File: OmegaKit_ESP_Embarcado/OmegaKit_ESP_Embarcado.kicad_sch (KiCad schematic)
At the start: 24 parts, among them J1 USB_B_Micro, J10 QTR_2, J11 SERVO1, J12 SERVO2, J2 MOTOR_B, J3 SENSOR_2, J4 SENSOR_1, J5 MOTOR_A, J6 SENSOR_3, J7 SENSOR_4, J8 SENSOR_5, J9 QTR_1, SW1 SW_Push, SW2 SW_Push, U1 CP2102N-Axx-xQFN28, U2 TB6612FNG, U3 ESP32-WROOM-32, U4 TSOP1838, U5 AMS1117-3.3

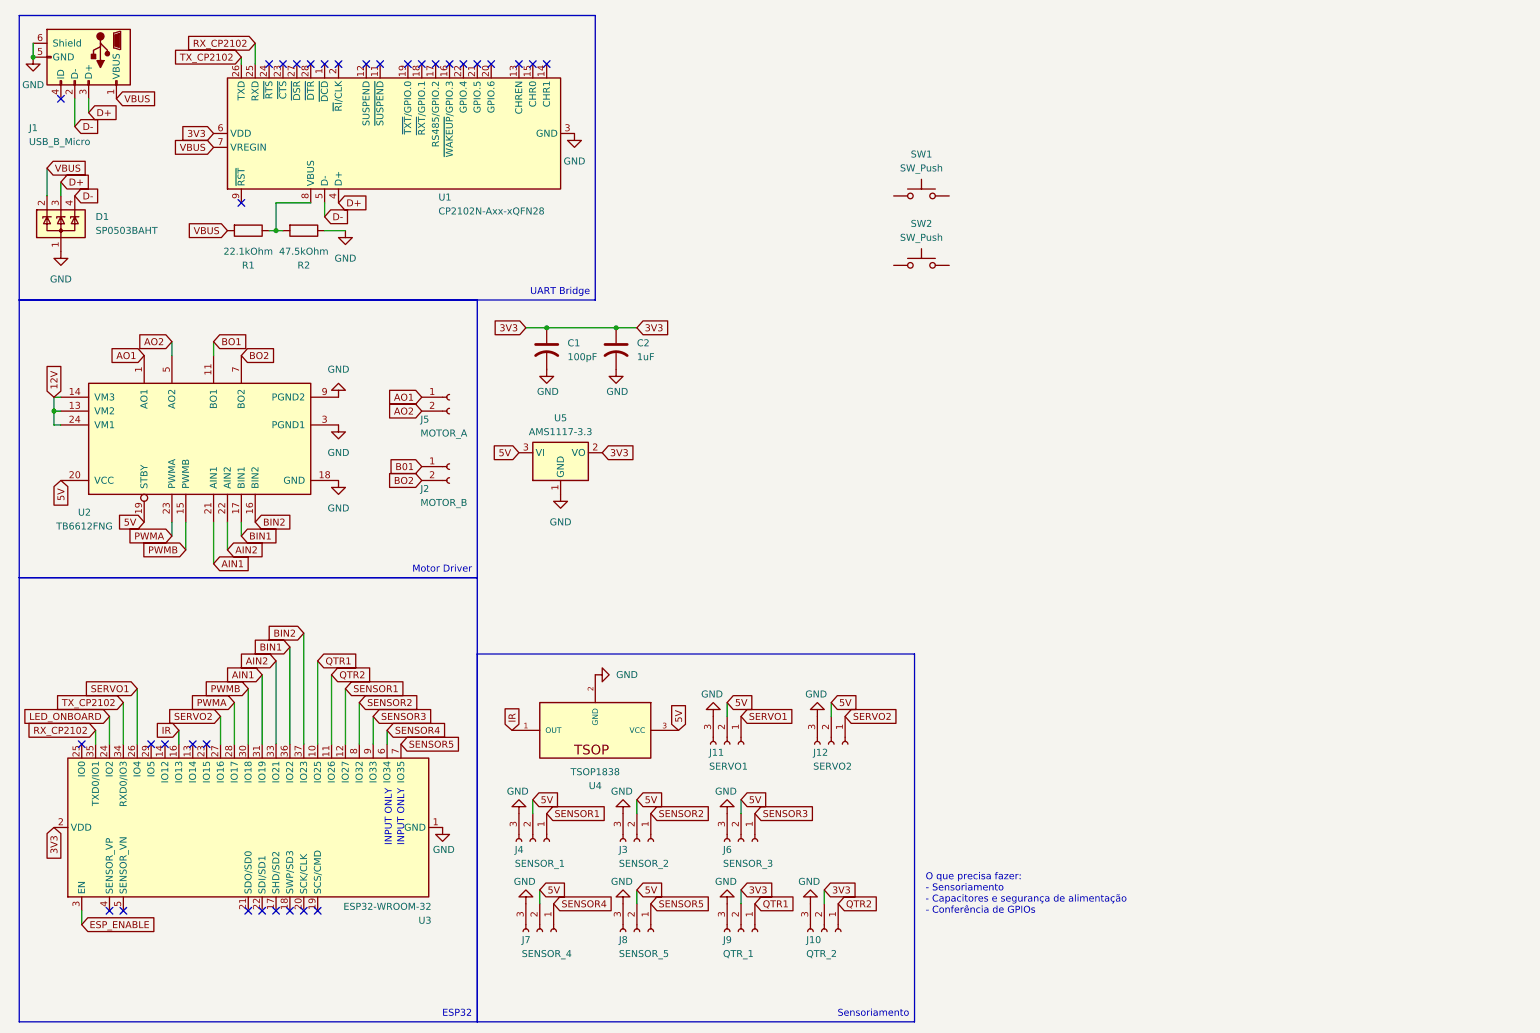
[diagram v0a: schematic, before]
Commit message: ✨🚧 feat(Omegakit_ESP_Embarcado/*): Inicia desenho da PCB
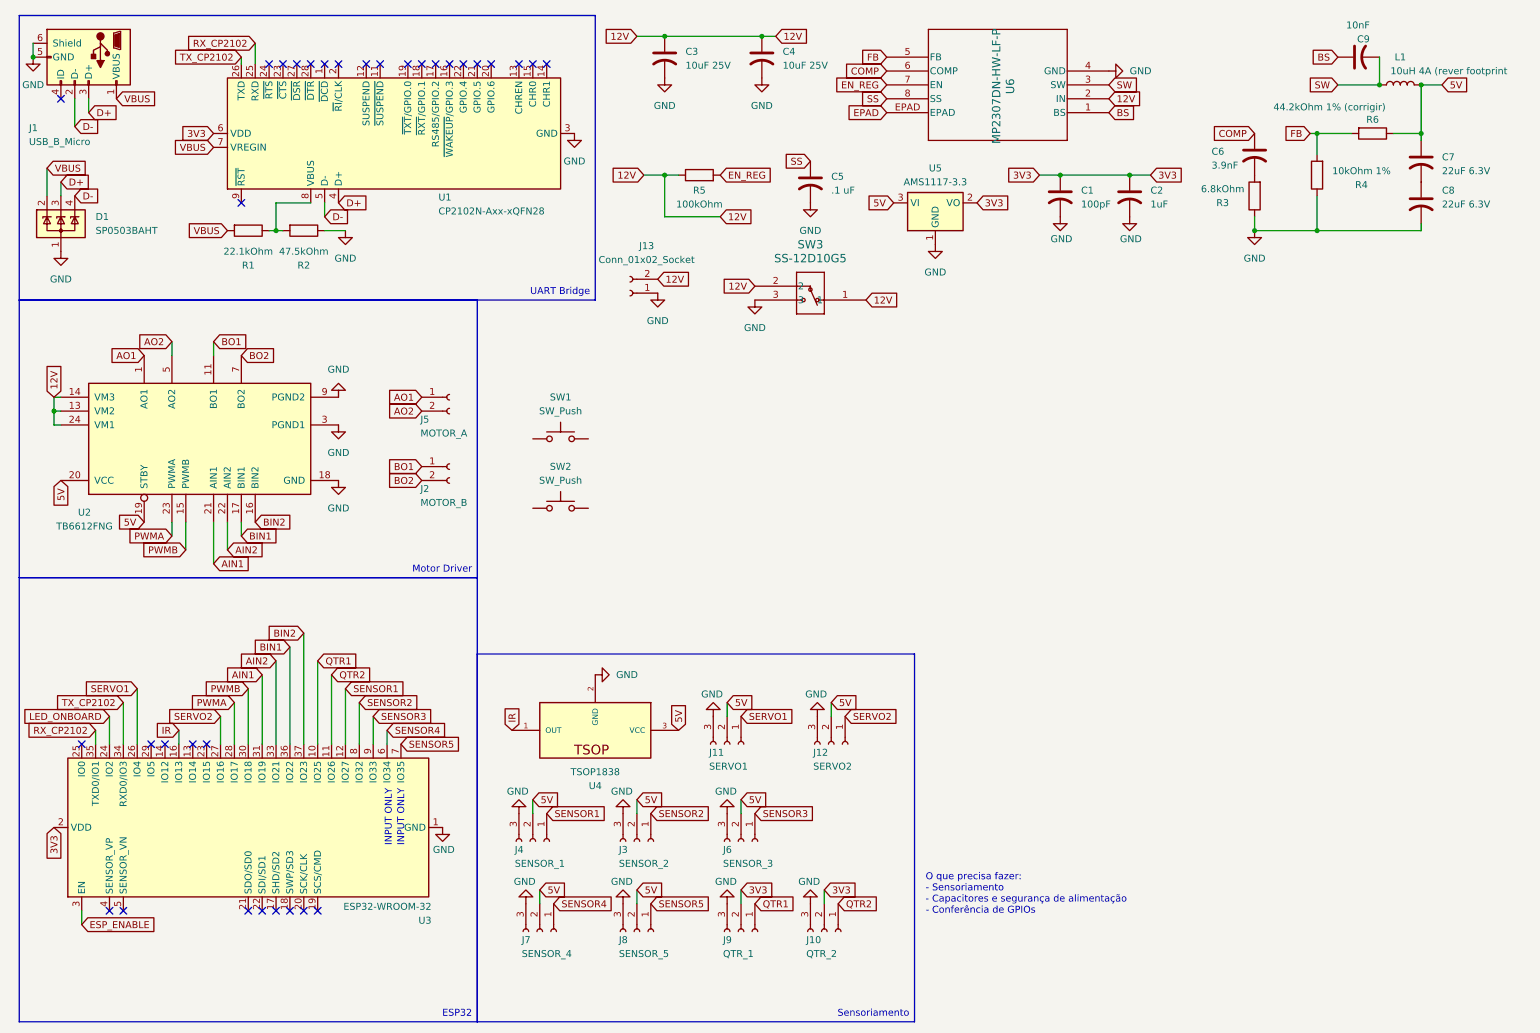
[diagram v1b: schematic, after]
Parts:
- added C3, C4: 10uF 25V, Capacitor_SMD:C_Elec_3x5.4, symbol Device:C_US
- added C5: .1 uF, Capacitor_SMD:C_0201_0603Metric_Pad0.64x0.40mm_HandSolder, symbol Device:C_US
- added C6: 3.9nF, Capacitor_SMD:C_0402_1005Metric_Pad0.74x0.62mm_HandSolder, symbol Device:C_US
- added C7, C8: 22uF 6.3V, Capacitor_SMD:C_1206_3216Metric_Pad1.33x1.80mm_HandSolder, symbol Device:C_US
- added C9: 10nF, Capacitor_SMD:C_0805_2012Metric_Pad1.18x1.45mm_HandSolder, symbol Device:C_US
- added J13: Conn_01x02_Socket, Connector_PinHeader_2.54mm:PinHeader_1x02_P2.54mm_Vertical, symbol Connector:Conn_01x02_Socket
- added L1: 10uH 4A (rever footprint, Inductor_SMD:L_Neosid_SM-PIC0512H, symbol Device:L
- added R3: 6.8kOhm, Resistor_SMD:R_0201_0603Metric_Pad0.64x0.40mm_HandSolder, symbol Device:R
- added R4: 10kOhm 1%, Resistor_SMD:R_0201_0603Metric_Pad0.64x0.40mm_HandSolder, symbol Device:R
- added R5: 100kOhm, Resistor_SMD:R_0201_0603Metric_Pad0.64x0.40mm_HandSolder, symbol Device:R
- added R6: 44.2kOhm 1% (corrigir), Resistor_SMD:R_0201_0603Metric_Pad0.64x0.40mm_HandSolder, symbol Device:R
- added SW3: SS-12D10G5, footprints:SS-12D10G5_XKB, symbol SS-12D10G5:SS-12D10G5
- added U6: MP2307DN-HW-LF-P, IC8_MP2307_MNP, symbol MP2307DN-HW-LF-P:MP2307DN-HW-LF-P
- C1: footprint (none) -> Capacitor_SMD:C_0603_1608Metric_Pad1.08x0.95mm_HandSolder
- C2: footprint (none) -> Capacitor_SMD:C_0402_1005Metric_Pad0.74x0.62mm_HandSolder
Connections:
- net B01 is gone; now on net BO1: J2.1 (Pin_1)
- net 12V: now also C3.1, C4.1, J13.2 (Pin_2), R5.1, SW3.1, SW3.2, U6.2 (IN)
- net 5V: now also C7.1, L1.2, R6.1
- net GND: now also C3.2, C4.2, C5.2, C8.2, J13.1 (Pin_1), R3.1, R4.1, SW3.3, U6.4 (GND)
- new net: C6.2, R3.2
- new net: C7.2, C8.1
- new net BS: C9.1, U6.1 (BS)
- new net COMP: C6.1, U6.6 (COMP)
- new net EN_REG: R5.2, U6.7 (EN)
- new net EPAD: U6.EPAD
- new net FB: R4.2, R6.2, U6.5 (FB)
- new net SS: C5.1, U6.8 (SS)
- new net SW: C9.2, L1.1, U6.3 (SW)
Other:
- moved on the sheet: C1, C2, SW1, SW2, U5

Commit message: ✨🚧 feat(OmegaKit_ESP_Embarcado/*): Monta primeira versão da placa, revisa circuitos, remove CP2102
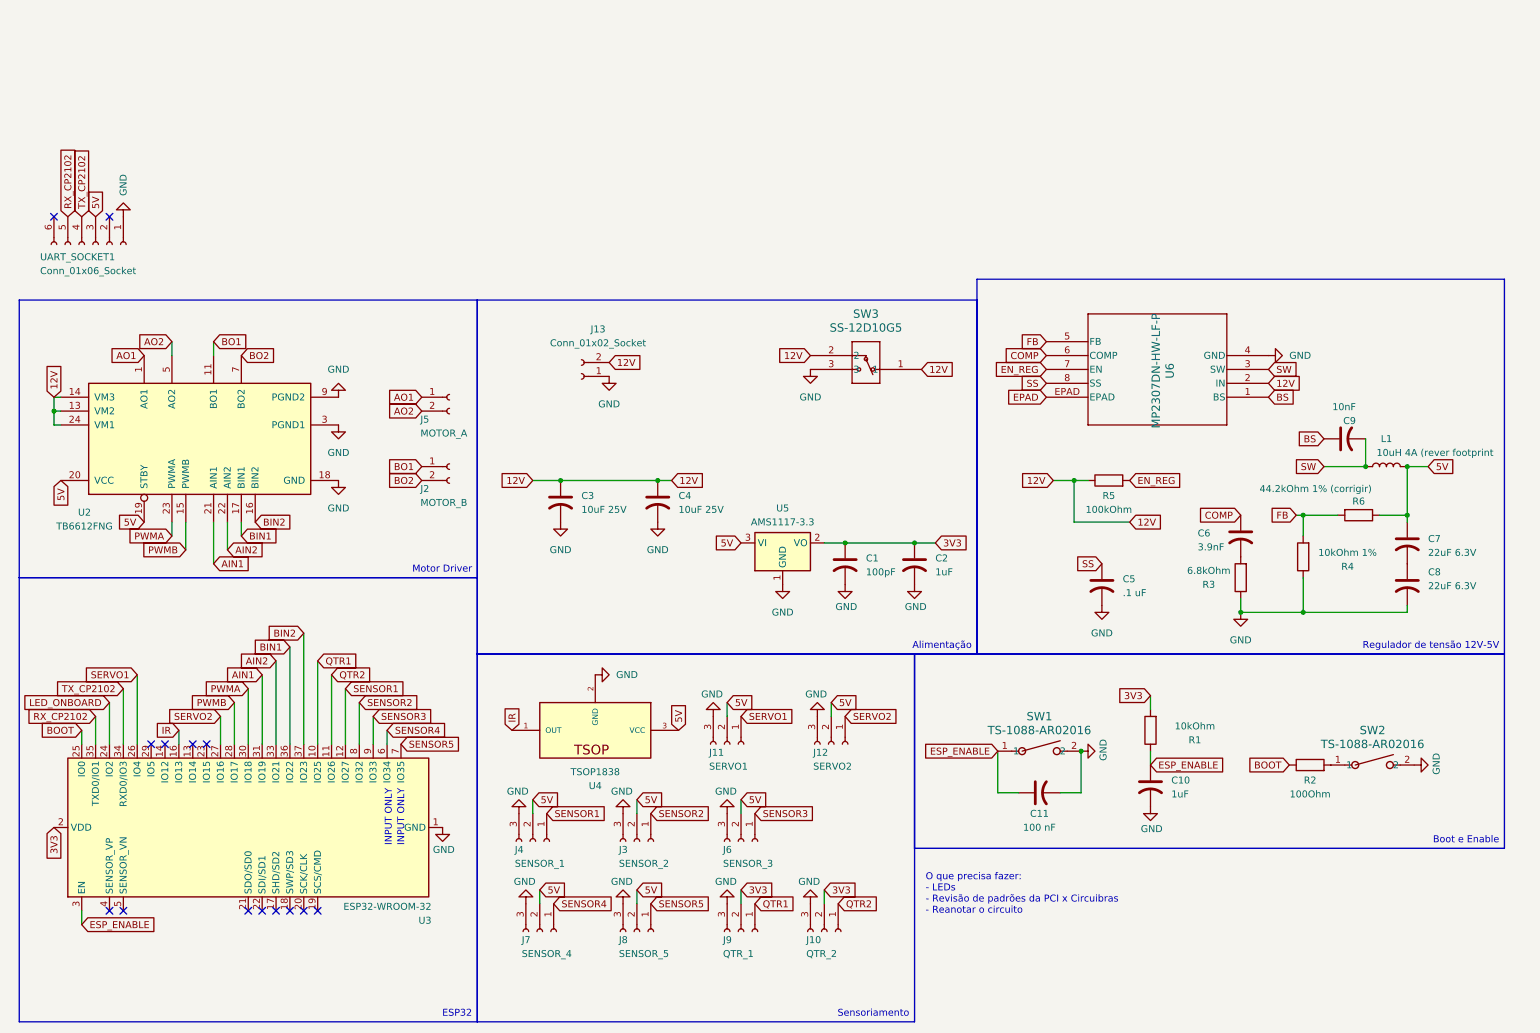
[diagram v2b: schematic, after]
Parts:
- removed D1: SP0503BAHT, Package_TO_SOT_SMD:SOT-143, symbol Power_Protection:SP0503BAHT
- removed J1: USB_B_Micro, Connector_USB:USB_Micro-AB_Molex_47590-0001, symbol Connector:USB_B_Micro
- removed SW1, SW2: SW_Push, symbol Switch:SW_Push
- removed U1: CP2102N-Axx-xQFN28, Package_DFN_QFN:QFN-28-1EP_5x5mm_P0.5mm_EP3.35x3.35mm, symbol Interface_USB:CP2102N-Axx-xQFN28
- added C10: 1uF, Capacitor_SMD:C_0402_1005Metric_Pad0.74x0.62mm_HandSolder, symbol Device:C_US
- added C11: 100 nF, Capacitor_SMD:C_0201_0603Metric_Pad0.64x0.40mm_HandSolder, symbol Device:C_US
- added SW1, SW2: TS-1088-AR02016, SW_TS-1088_XNP, symbol TS-1088-ARO2016:TS-1088-AR02016
- added UART_SOCKET1: Conn_01x06_Socket, Connector_PinHeader_2.54mm:PinHeader_1x06_P2.54mm_Vertical, symbol Connector:Conn_01x06_Socket
- C7, C8: footprint Capacitor_SMD:C_1206_3216Metric_Pad1.33x1.80mm_HandSolder -> Capacitor_SMD:C_0603_1608Metric_Pad1.08x0.95mm_HandSolder
- C9: footprint Capacitor_SMD:C_0805_2012Metric_Pad1.18x1.45mm_HandSolder -> Capacitor_SMD:C_0504_1310Metric_Pad0.83x1.28mm_HandSolder
- R1: value 22.1kOhm -> 10kOhm; footprint Resistor_SMD:R_0201_0603Metric_Pad0.64x0.40mm_HandSolder -> Resistor_SMD:R_0603_1608Metric_Pad0.98x0.95mm_HandSolder
- R2: value 47.5kOhm -> 100Ohm; footprint Resistor_SMD:R_0201_0603Metric_Pad0.64x0.40mm_HandSolder -> Resistor_SMD:R_0805_2012Metric_Pad1.20x1.40mm_HandSolder
- R4, R6: footprint Resistor_SMD:R_0201_0603Metric_Pad0.64x0.40mm_HandSolder -> Resistor_SMD:R_0603_1608Metric_Pad0.98x0.95mm_HandSolder
- R5: footprint Resistor_SMD:R_0201_0603Metric_Pad0.64x0.40mm_HandSolder -> Resistor_SMD:R_0805_2012Metric_Pad1.20x1.40mm_HandSolder
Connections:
- net VBUS is gone; now on net 3V3: R1.2
- net 5V: now also UART_SOCKET1.3 (Pin_3)
- net ESP_ENABLE: now also R1.1, C10.1, C11.1, SW1.1
- net GND: now also C10.2, C11.2, SW1.2, SW2.2, UART_SOCKET1.1 (Pin_1); no longer R2.1
- net PWMA: now also U3.30 (IO18); no longer U3.28 (IO17)
- net PWMB: now also U3.28 (IO17); no longer U3.30 (IO18)
- net RX_CP2102: now also UART_SOCKET1.5 (Pin_5)
- net TX_CP2102: now also UART_SOCKET1.4 (Pin_4)
- net at R2.2: now also SW2.1; no longer R1.1
- net BOOT: now reaches U3.25 (IO0)
- net BOOT: now also R2.1
- no-connect marks 33 -> 14
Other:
- note added: "O que precisa fazer: - LEDs - Revisão de padrões da PCI x Circuibras - Reanotar o circuito"
- note removed: "O que precisa fazer: - Sensoriamento - Capacitores e segurança de alimentação - Conferência de GPIOs"
- moved on the sheet: C1, C2, C3, C4, C5, C6, C7, C8, C9, J13, L1, R3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

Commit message: ✨ feat(OmegaKit_ESP_Embarcado/*): Adiciona LEDs nos sensores e LED de energia, muda footprint dos capacitores da bateria
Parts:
- added D1, D2, D3, D4, D5, D6, D7: LED, LED_SMD:LED_0805_2012Metric_Pad1.15x1.40mm_HandSolder, symbol Device:LED
- added R10, R11, R12, R7, R8, R9: 220Ohm, Resistor_SMD:R_0805_2012Metric_Pad1.20x1.40mm_HandSolder, symbol Device:R
- added R13: 1KOhm, Resistor_SMD:R_0805_2012Metric_Pad1.20x1.40mm_HandSolder, symbol Device:R
- C1: renamed from C3; footprint Capacitor_SMD:C_Elec_3x5.4 -> Capacitor_SMD:C_Elec_4x5.4
- C2: renamed from C4; footprint Capacitor_SMD:C_Elec_3x5.4 -> Capacitor_SMD:C_Elec_4x5.4
- renumbered C1 to C3, C2 to C4, U4 to IR13, J9 to Q25, J10 to Q26, J4 to S27, J3 to S32, J6 to S33, J7 to S34, J8 to S35, J12 to SERVO16, J11 to SERVO4
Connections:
- net 3V3: now also R13.1
- net GND: now also D1.1 (K), D7.1 (K)
- net LED_ONBOARD: now also R7.1
- net SENSOR1: now also D2.1 (K), R8.1
- net SENSOR2: now also D4.1 (K), R10.1
- net SENSOR3: now also D6.1 (K), R12.1
- net SENSOR4: now also D5.1 (K), R11.1
- net SENSOR5: now also D3.1 (K), R9.1
- new net: D4.2 (A), R10.2
- new net: D5.2 (A), R11.2
- new net: D6.2 (A), R12.2
- new net: D3.2 (A), R9.2
- new net: D2.2 (A), R8.2
- new net: D7.2 (A), R13.2
- new net: D1.2 (A), R7.2
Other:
- note added: "O que precisa fazer: - Rever padrões Circuibras - Rever valores (fazer contaKKKKKKKKKKKKKKK)"
- note removed: "O que precisa fazer: - LEDs - Revisão de padrões da PCI x Circuibras - Reanotar o circuito"

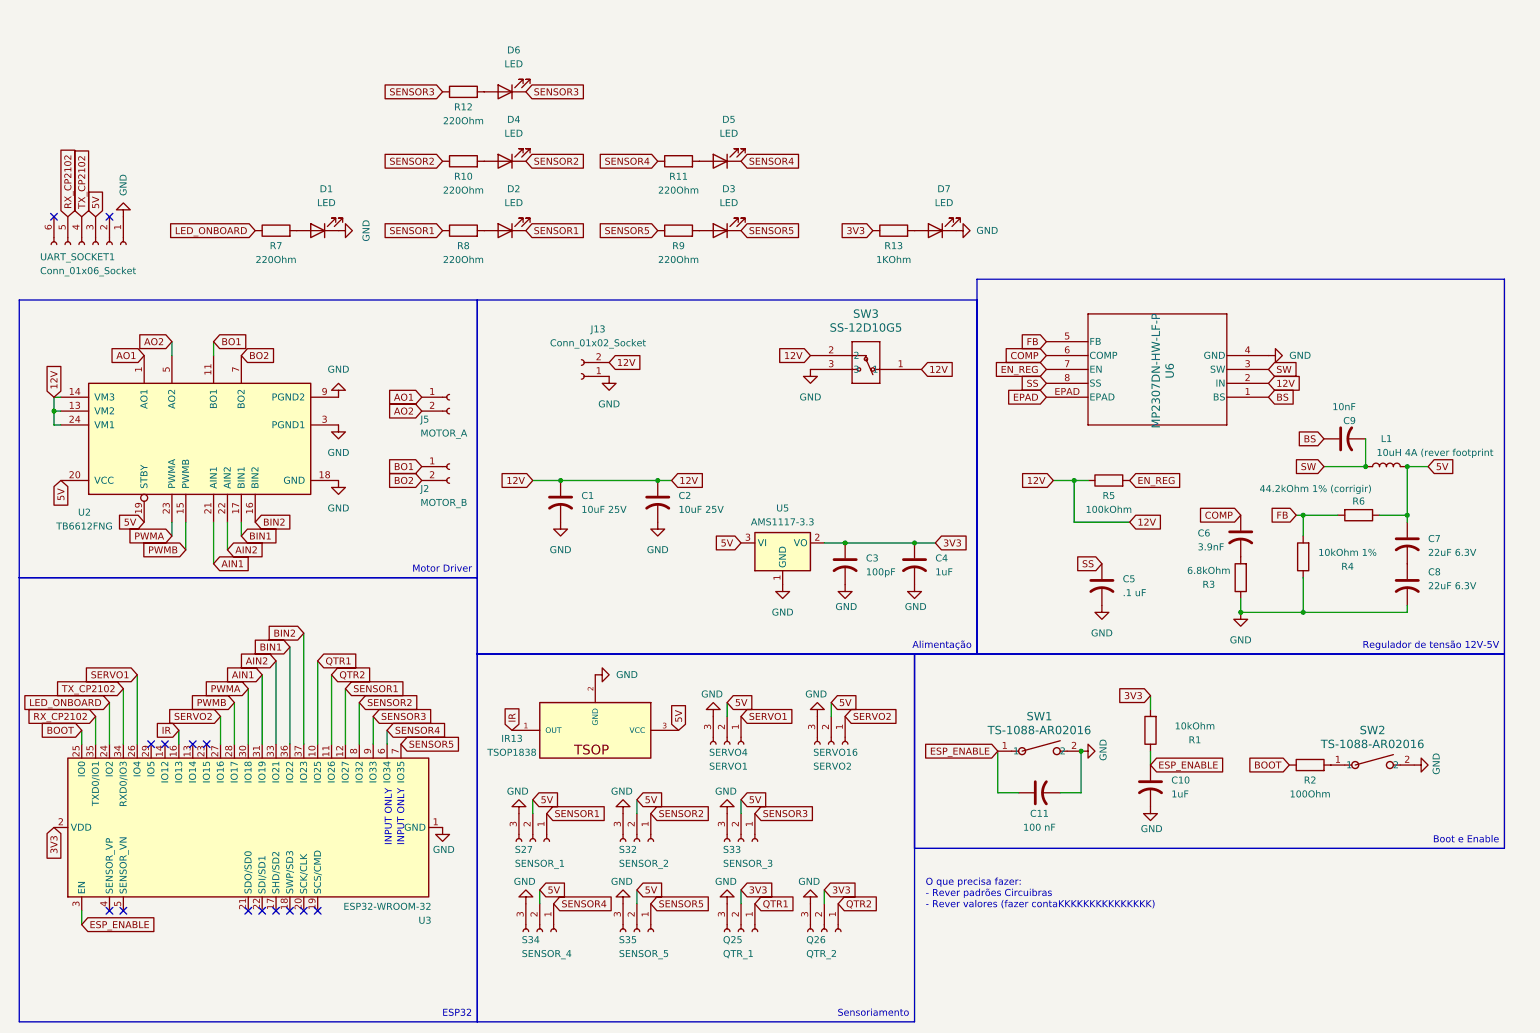
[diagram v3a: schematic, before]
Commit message: 🧹 chore(OmegaKit_ESP_Embarcado/*): Reorganiza projeto, plota projeto em PDF
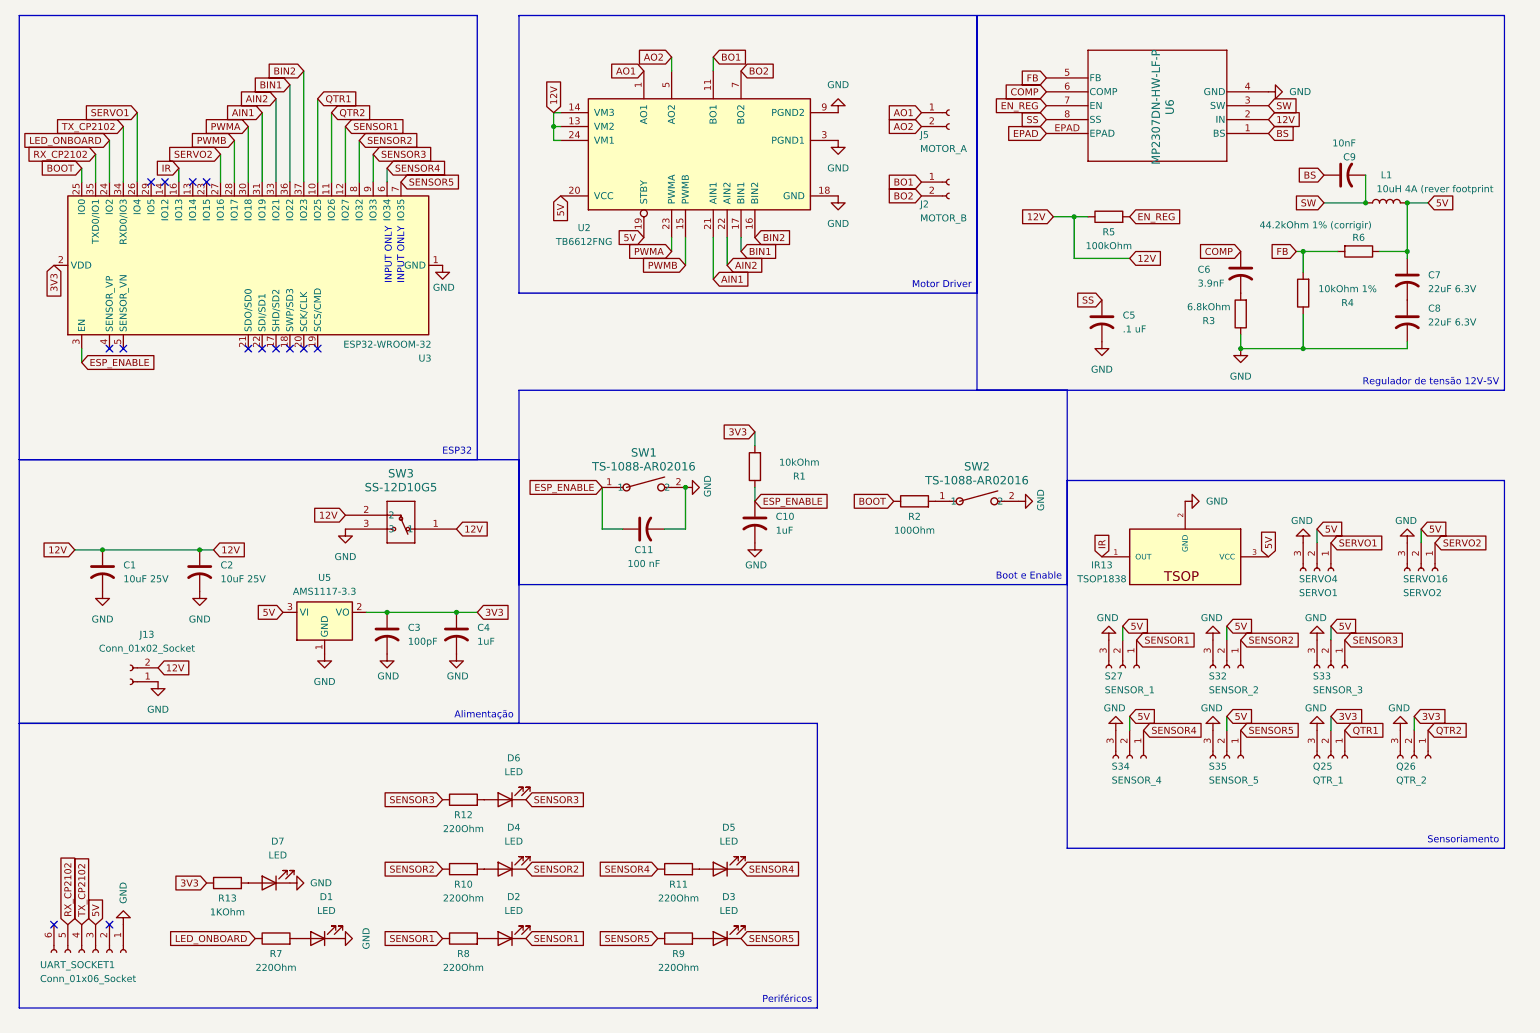
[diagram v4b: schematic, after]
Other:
- note removed: "O que precisa fazer: - Rever padrões Circuibras - Rever valores (fazer contaKKKKKKKKKKKKKKK)"
- moved on the sheet: C1, C10, C11, C2, C3, C4, C5, C6, C7, C8, C9, D1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
